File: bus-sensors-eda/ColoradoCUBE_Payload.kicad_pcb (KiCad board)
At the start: 2 copper layers, 96.5 x 90.7 mm, 58 parts, among them J1 Conn_02x20_Odd_Even, J2 Conn_01x06, J3 Conn_01x06, J4 Conn_01x04, J5 Conn_01x02, J6 Conn_01x02, J7 Conn_01x02, J8 Conn_01x04, SW1 SW_SPST, U1 PIC18F27Q84-E/SP, U2 SHT40-AD1B-R2, U3 ATA6560-GAQW-VAO, U4 MS580502BA01-50, U5 TMP75CIDGKT

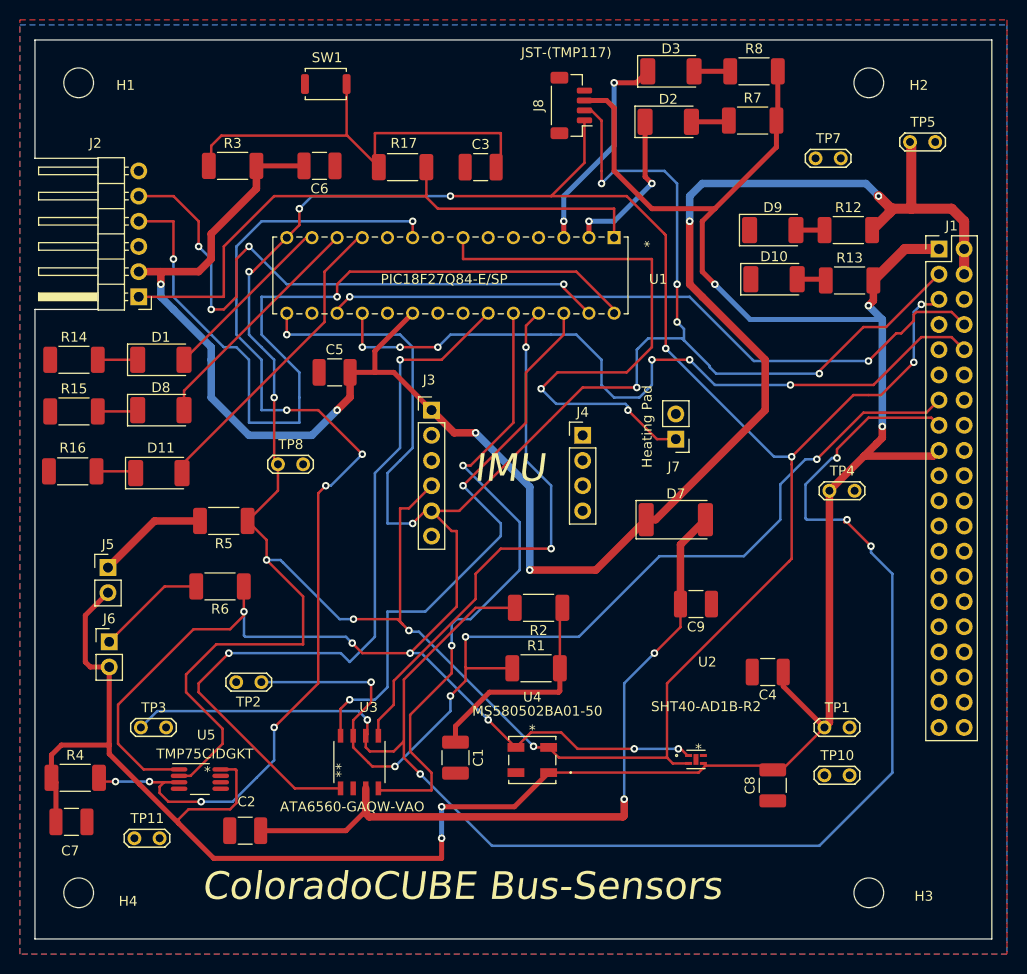
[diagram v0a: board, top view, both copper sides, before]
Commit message: courtyards and silkscreens correction
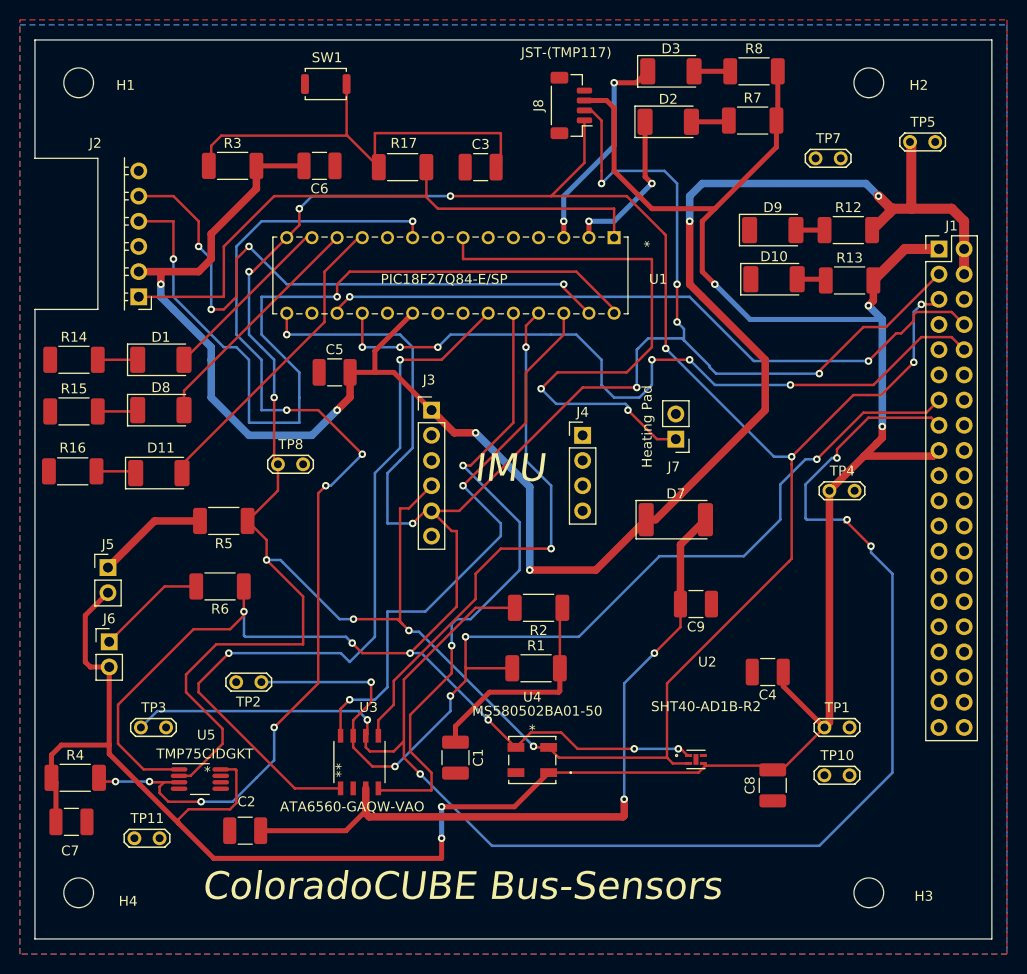
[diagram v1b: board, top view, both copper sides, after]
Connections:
- J1 pad 11: GND -> unconnected-(J1-Pad11)
- J1 pad 12: GND -> unconnected-(J1-Pad12)
- J1 pad 14: GND -> unconnected-(J1-Pad14)
- J1 pad 16: GND -> unconnected-(J1-Pad16)
- J1 pad 18: GND -> unconnected-(J1-Pad18)
- J1 pad 19: GND -> unconnected-(J1-Pad19)
- J1 pad 21: GND -> unconnected-(J1-Pad21)
- J1 pad 22: GND -> unconnected-(J1-Pad22)
- J1 pad 23: GND -> unconnected-(J1-Pad23)
- J1 pad 24: GND -> unconnected-(J1-Pad24)
- J1 pad 26: GND -> unconnected-(J1-Pad26)
- J1 pad 27: GND -> unconnected-(J1-Pad27)
- J1 pad 28: GND -> unconnected-(J1-Pad28)
- J1 pad 29: GND -> unconnected-(J1-Pad29)
- J1 pad 31: GND -> unconnected-(J1-Pad31)
- J1 pad 32: GND -> unconnected-(J1-Pad32)
- J1 pad 33: GND -> unconnected-(J1-Pad33)
- J1 pad 35: GND -> unconnected-(J1-Pad35)
- J1 pad 36: GND -> unconnected-(J1-Pad36)
- J1 pad 37: GND -> unconnected-(J1-Pad37)
- J1 pad 38: GND -> unconnected-(J1-Pad38)
- J1 pad 40: GND -> unconnected-(J1-Pad40)
- J1 pad 7: GND -> unconnected-(J1-Pad7)
